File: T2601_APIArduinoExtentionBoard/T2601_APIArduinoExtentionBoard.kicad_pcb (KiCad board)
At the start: 4 copper layers, 59.8 x 90 mm, 100 parts, among them J1 Conn_01x10_Socket, J11 Conn_01x04_Pin, J12 Screw_Terminal_01x02, J13 Conn_01x04_Pin, J14 Screw_Terminal_01x02, J15 Conn_02x08_Counter_Clockwise, J2 Conn_01x10_Socket, J3 Conn_01x10_Socket, J4 Conn_01x10_Socket, J5 Screw_Terminal_01x08, J6 Screw_Terminal_01x08, J7 Conn_02x03_Counter_Clockwise, J8 Conn_01x04, J9 Conn_02x08_Counter_Clockwise, U2 ATmega328PB-A, X1 X322516MOB4SI

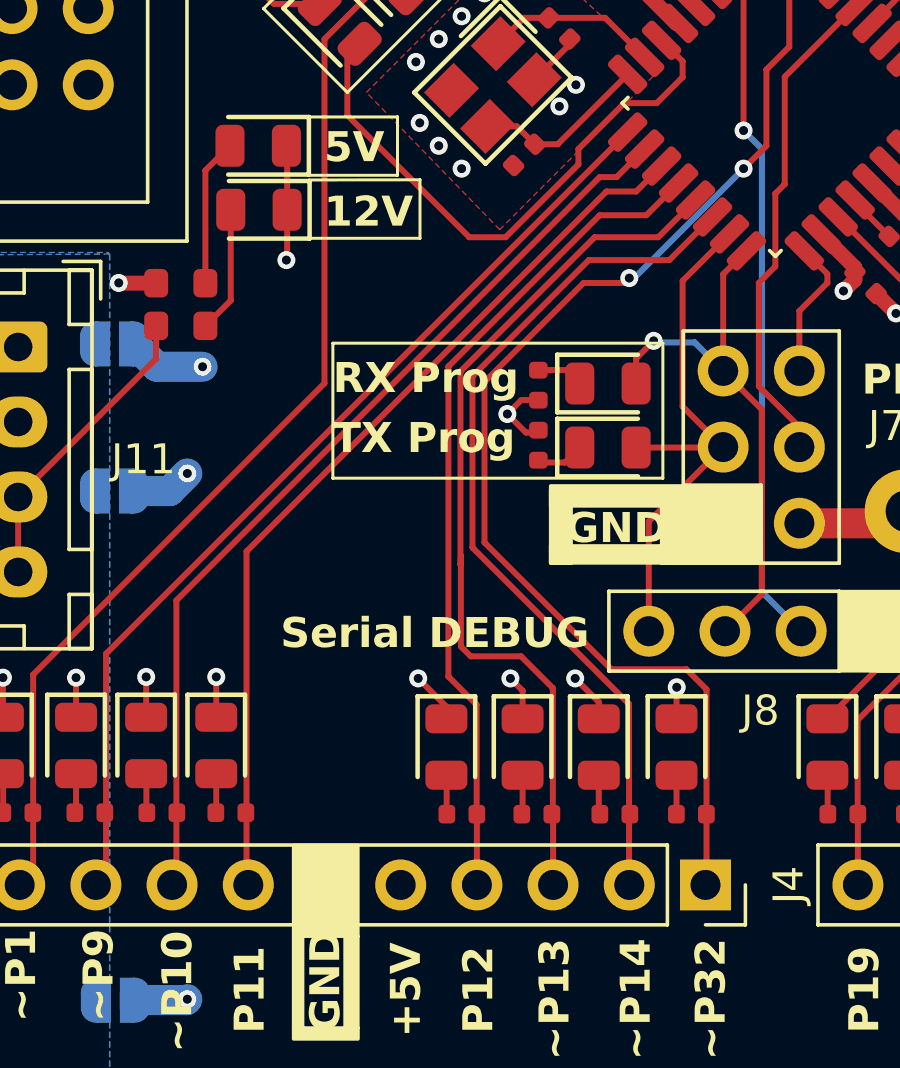
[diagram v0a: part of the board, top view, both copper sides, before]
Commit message: Modification affectation pin PWM Mezz 1
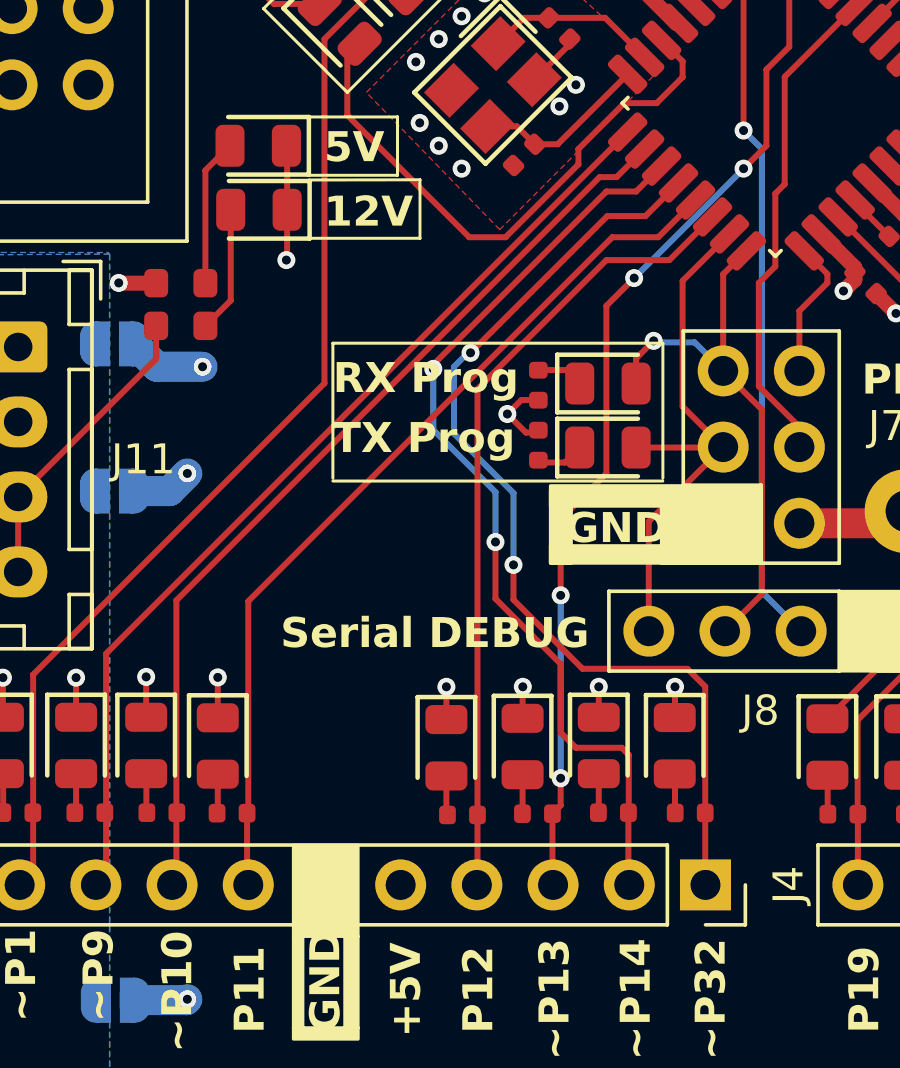
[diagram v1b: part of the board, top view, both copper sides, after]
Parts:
- moved D14 12.8 mm to (150.1, 78.4)
- moved R10 12.8 mm to (150.6, 80.7)
- moved D16 10.2 mm to (137.4, 78.4)
- moved R12 10.2 mm to (137.9, 80.7)
- moved D15 7.61 mm to (152.6, 78.4)
- moved R11 7.61 mm to (153.2, 80.7)
- moved D18 5.13 mm to (147.6, 78.4)
- moved R14 5.13 mm to (148.1, 80.7)
- moved D17 5.08 mm to (145.0, 78.5)
- moved R13 5.08 mm to (145.6, 80.7)
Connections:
- J4 pad 1: P32 -> P12
- J4 pad 2: P14 -> P11
- J4 pad 3: P13 -> P32
- J4 pad 4: P12 -> P14
- J4 pad 7: P11 -> P13
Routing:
- net P32: track 40.8 -> 34.5 mm, vias 2 -> 4
- net P12: track 27.9 -> 32.9 mm, vias 0 -> 2
- net P14: track 29.3 -> 26.7 mm
- net GND: track 79.5 -> 77.7 mm
- net P11: track 30.3 -> 31.3 mm, vias 0 -> 2

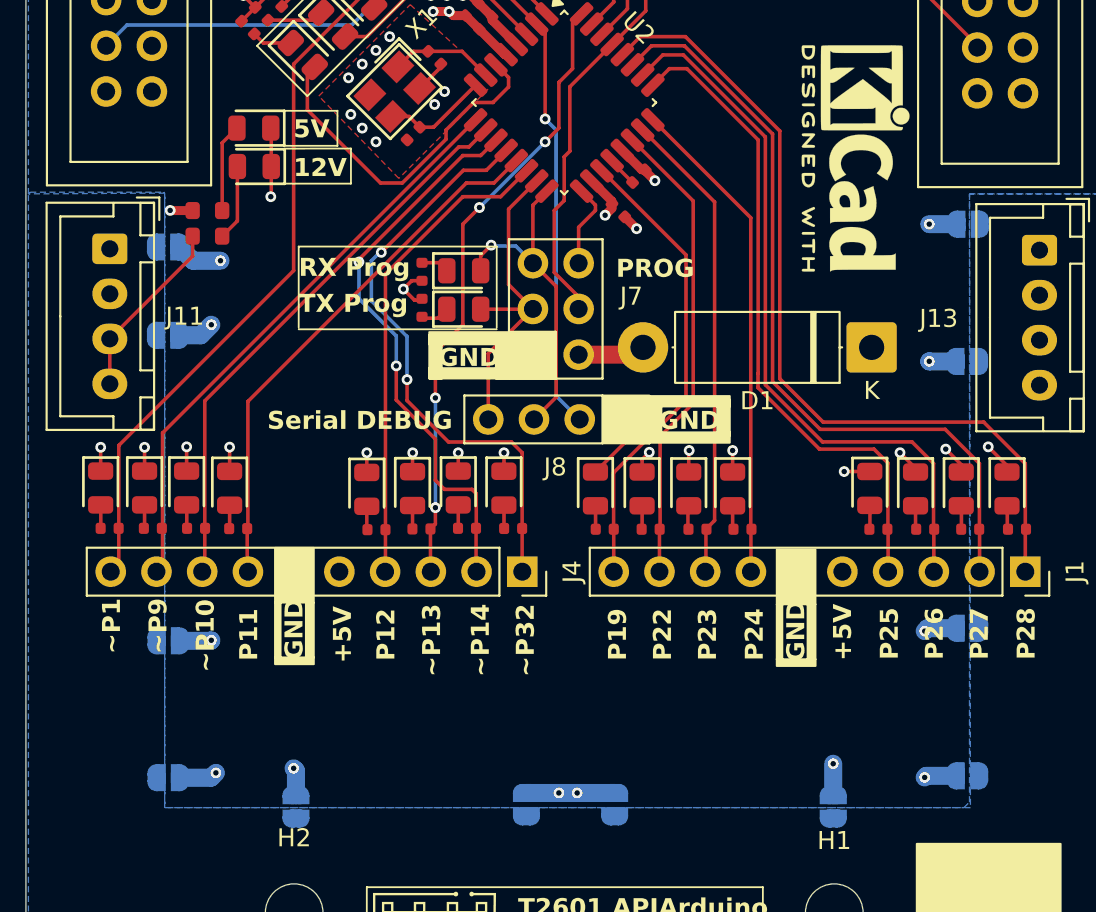
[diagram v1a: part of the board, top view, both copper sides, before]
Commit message: Modification issue #20 GND de la led 12V + ajout via entre In.1 et Bot pour la liaison des couches de GND
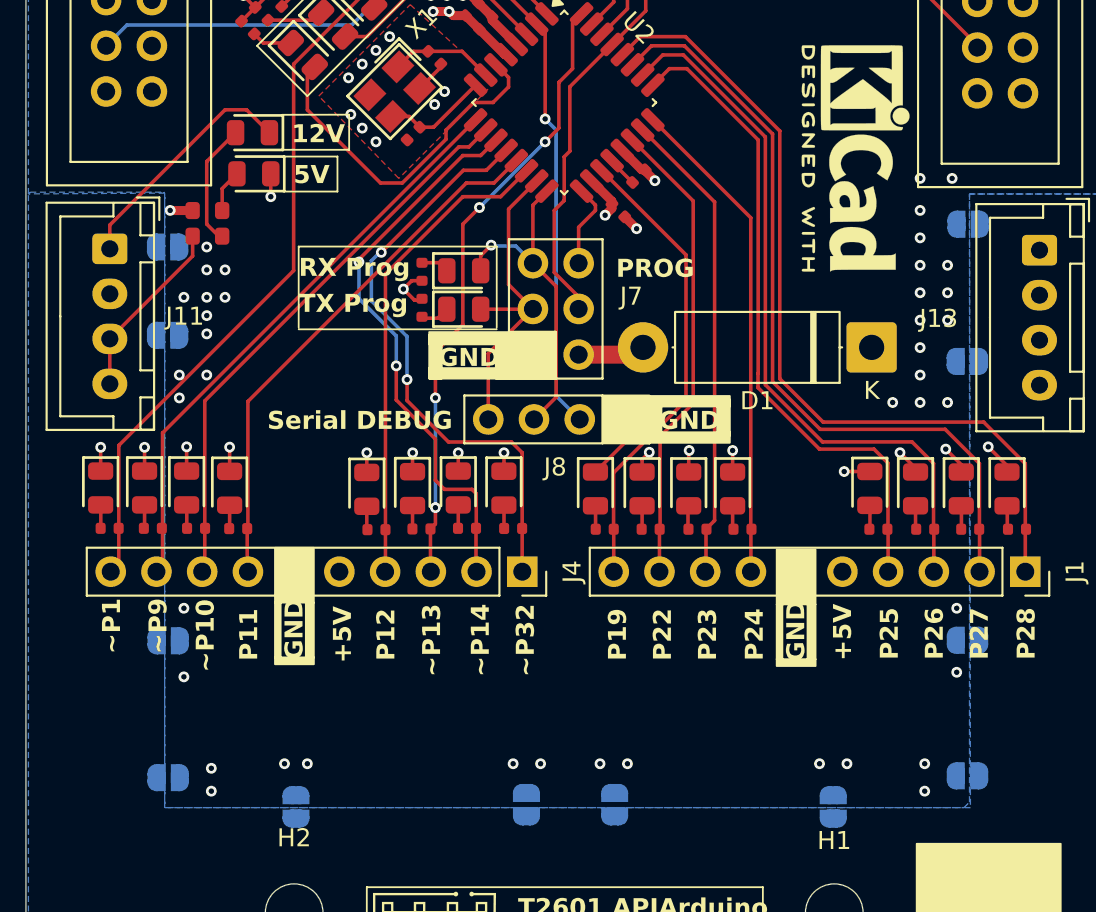
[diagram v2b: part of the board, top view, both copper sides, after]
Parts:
- moved D8 2.54 mm to (138.8, 61.0)
- moved D7 1.88 mm to (138.7, 58.7)
- moved JP7 0.67 mm to (178.4, 86.9)
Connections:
- D7 pad 1: GND -> GNDPWR
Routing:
- net GND: track 77.7 -> 51.9 mm, vias 45 -> 75
- net GNDPWR: track 0.00 -> 13.4 mm
- net Net-(D7-Pad2): track 4.22 -> 6.88 mm
- net Net-(D8-Pad2): track 4.92 -> 2.38 mm

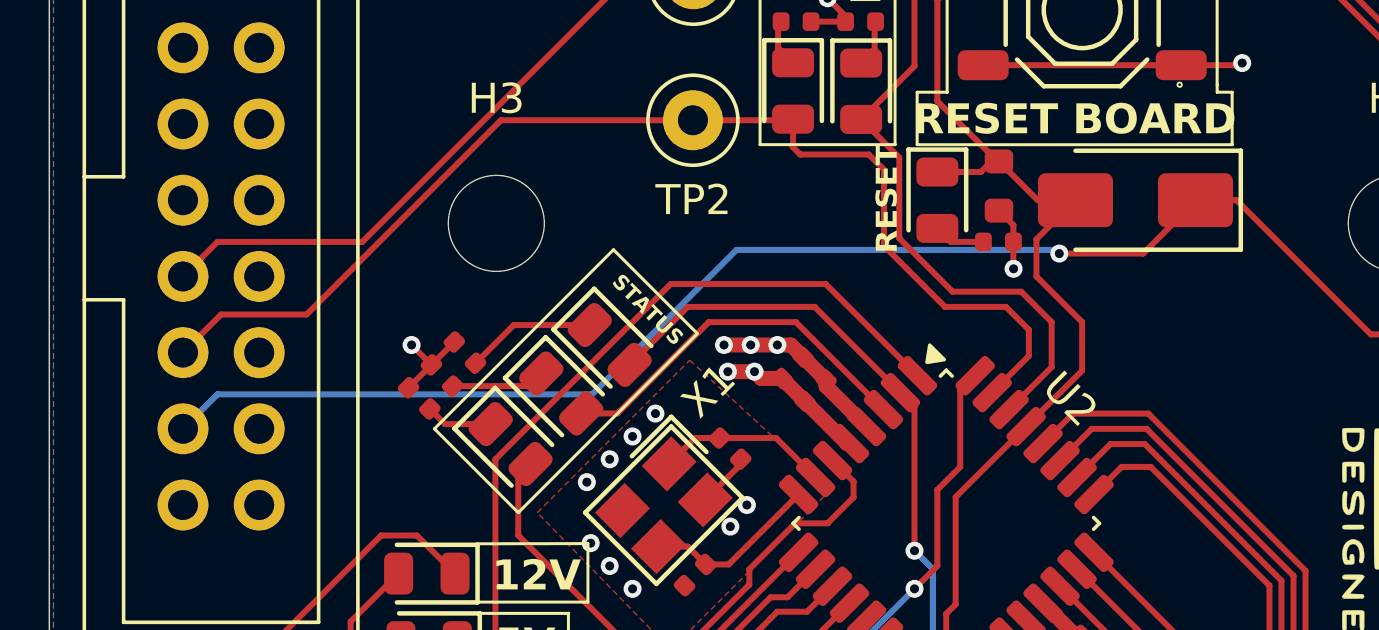
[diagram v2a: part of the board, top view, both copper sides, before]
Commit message: Piste de RESET general
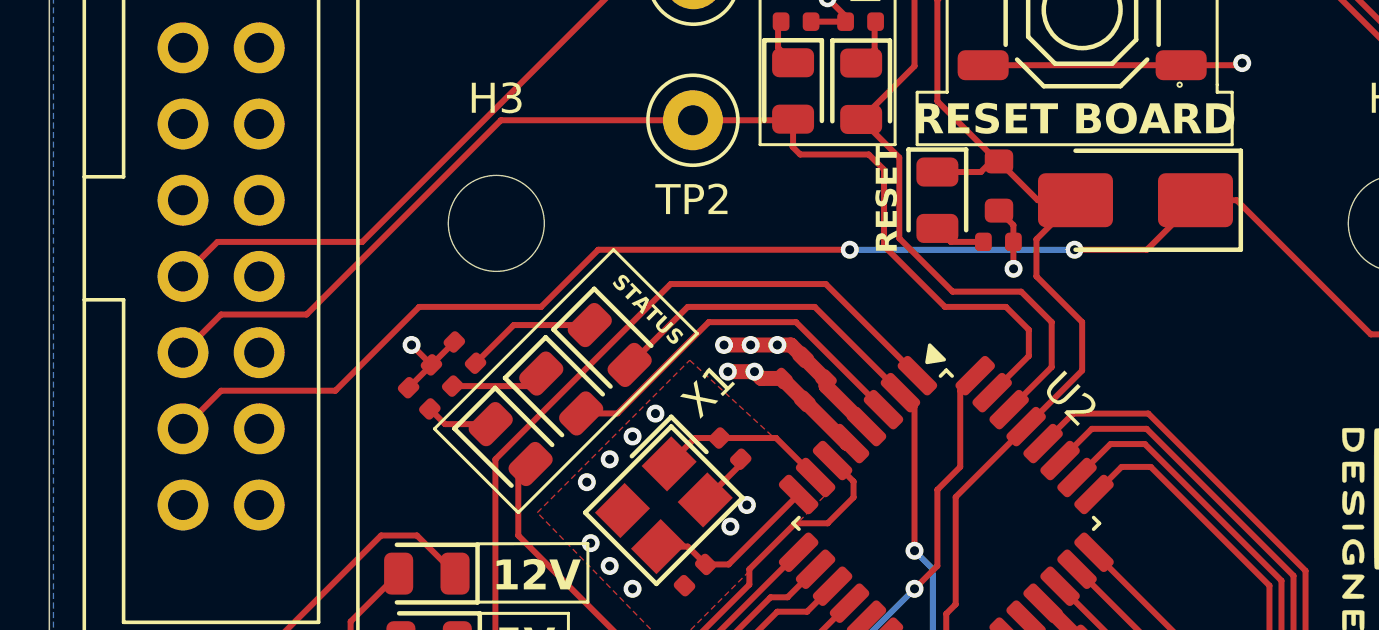
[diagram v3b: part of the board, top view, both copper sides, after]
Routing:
- net GEN_RESET: track 54.9 -> 54.8 mm, vias 1 -> 2
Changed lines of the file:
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@@
+	)
+	(segment
+		(start 160.274 47.879)
+		(end 162.687 47.879)
+		(width 0.2)
+		(layer "F.Cu")
+		(net "GEN_RESET")
+	)
+	(segment
+		(start 144.399 47.879)
+		(end 152.781 47.879)
+		(width 0.2)
+		(layer "F.Cu")
+		(net "GEN_RESET")
 	)
 	(segment
@@
 	)
 	(segment
-		(start 162.56 48.006)
-		(end 159.766 48.006)
+		(start 138.43 49.784)
+		(end 142.494 49.784)
+		(width 0.2)
+		(layer "F.Cu")
+		(net "GEN_RESET")
+	)
+	(segment
+		(start 142.494 49.784)
+		(end 144.399 47.879)
 		(width 0.2)
 		(layer "F.Cu")
@@
 	(segment
 		(start 164.306001 46.259999)
-		(end 162.56 48.006)
+		(end 162.687 47.879)
 		(width 0.2)
 		(layer "F.Cu")
@@
 		(start 170.15 50.7)
 		(end 165.678 46.228)
+		(width 0.2)
+		(layer "F.Cu")
+		(net "GEN_RESET")
+	)
+	(segment
+		(start 130.556 53.848)
+		(end 131.826 52.578)
+		(width 0.2)
+		(layer "F.Cu")
+		(net "GEN_RESET")
+	)
+	(segment
+		(start 131.826 52.578)
+		(end 135.636 52.578)
 		(width 0.2)
 		(layer "F.Cu")
@@
 	)
 	(segment
+		(start 135.636 52.578)
+		(end 138.43 49.784)
+		(width 0.2)
+		(layer "F.Cu")
+		(net "GEN_RESET")
+	)
+	(segment
 		(start 165.678 46.228)
 		(end 164.306001 46.228)
@@
 	)
 	(via
-		(at 159.766 48.006)
+		(at 152.781 47.879)
+		(size 0.6)
+		(drill 0.3)
+		(layers "F.Cu" "B.Cu")
+		(net "GEN_RESET")
+	)
+	(via
+		(at 160.274 47.879)
 		(size 0.6)
 		(drill 0.3)
@@
 	)
 	(segment
-		(start 131.706 52.698)
-		(end 130.556 53.848)
+		(start 152.781 47.879)
+		(end 160.274 47.879)
 		(width 0.2)
 		(layer "B.Cu")
-		(net "GEN_RESET")
-	)
-	(segment
-		(start 144.192471 52.698)
-		(end 131.706 52.698)
-		(width 0.2)
-		(layer "B.Cu")
-		(net "GEN_RESET")
-	)
-	(segment
-		(start 149.006096 47.884375)
-		(end 144.192471 52.698)
-		(width 0.2)
-		(layer "B.Cu")
-		(net "GEN_RESET")
-	)
-	(segment
-		(start 159.766 48.006)
-		(end 159.644375 47.884375)
-		(width 0.2)
-		(layer "B.Cu")
-		(net "GEN_RESET")
-	)
-	(segment
-		(start 159.644375 47.884375)
-		(end 149.006096 47.884375)
-		(width 0.2)
-		(layer "B.Cu")

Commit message: Modification connecteurs
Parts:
- renumbered J7 to J10, J8 to J11, J4 to J2, J15 to J20, J9 to J21, J11 to J30, J13 to J31, J2 to J4

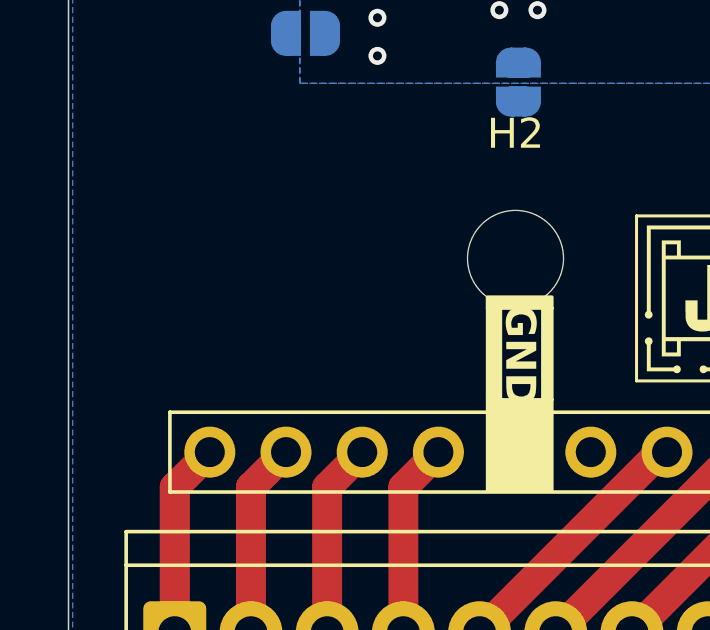
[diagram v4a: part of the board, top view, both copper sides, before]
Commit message: Ajouter Layer registration window
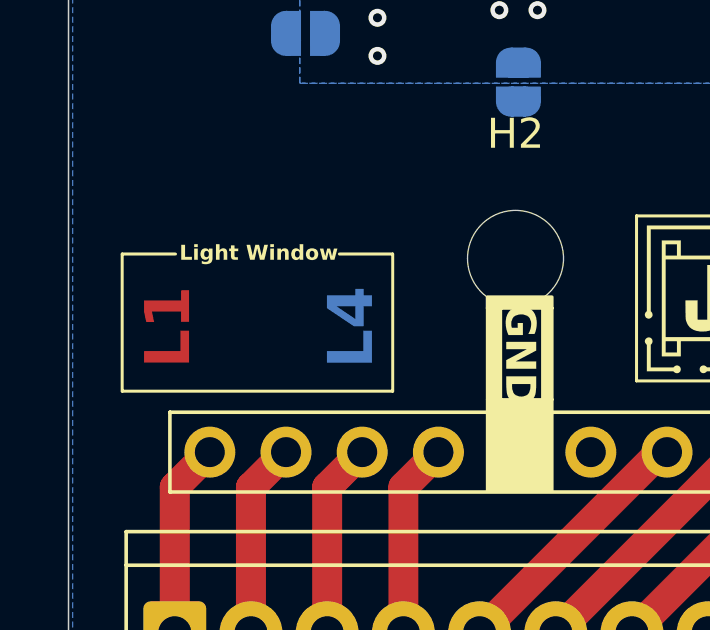
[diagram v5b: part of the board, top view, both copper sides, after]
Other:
- board text added: "L1"
- board text added: "L2"
- board text added: "L3"
- board text added: "L4"
- board text added: "Light Window"
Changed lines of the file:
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@@
 		)
 		(property "Value" "SolderJumper_2_Open"
-			(at 0 -1.9 0)
+			(at 6.230999 -7.212 90)
 			(layer "B.Fab")
 			(effects
@@
 	)
 	(gr_line
+		(start 127.889 101.854)
+		(end 127.889 106.426)
+		(stroke
+			(width 0.1)
+			(type default)
+		)
+		(layer "F.SilkS")
+	)
+	(gr_line
+		(start 127.889 106.426)
+		(end 136.906 106.426)
+		(stroke
+			(width 0.1)
+			(type default)
+		)
+		(layer "F.SilkS")
+	)
+	(gr_line
+		(start 129.667 101.854)
+		(end 127.889 101.854)
+		(stroke
+			(width 0.1)
+			(type default)
+		)
+		(layer "F.SilkS")
+	)
+	(gr_line
+		(start 135.128 101.854)
+		(end 136.906 101.854)
+		(stroke
+			(width 0.1)
+			(type default)
+		)
+		(layer "F.SilkS")
+	)
+	(gr_line
+		(start 136.906 101.854)
+		(end 136.906 106.426)
+		(stroke
+			(width 0.1)
+			(type default)
+		)
+		(layer "F.SilkS")
+	)
+	(gr_line
 		(start 138.938 53.848)
 		(end 144.907 47.879)
@@
 		(layer "Edge.Cuts")
 	)
+	(gr_text "L1\n"
+		(at 130.302 105.664 90)
+		(layer "F.Cu")
+		(effects
+			(font
+				(size 1.5 1.5)
+				(thickness 0.3)
+				(bold yes)
+			)
+			(justify left bottom)
+		)
+	)
 	(gr_text "\nCopyright (C) 2026 HackHype\nCERN OHL-S v2\n\n"
 		(at 154.91 37.72 0)
@@
 		)
 	)
+	(gr_text "L4\n"
+		(at 136.398 105.664 90)
+		(layer "B.Cu")
+		(effects
+			(font
+				(size 1.5 1.5)
+				(thickness 0.3)
+				(bold yes)
+			)
+			(justify left bottom)
+		)
+	)
+	(gr_text "L2\n"
+		(at 132.334 105.664 90)
+		(layer "In1.Cu")
+		(effects
+			(font
+				(size 1.5 1.5)
+				(thickness 0.3)
+				(bold yes)
+			)
+			(justify left bottom)
+		)
+	)
+	(gr_text "Light Window"
+		(at 129.794 102.108 0)
+		(layer "F.SilkS")
+		(effects
+			(font
+				(size 0.5 0.5)
+				(thickness 0.125)
+				(bold yes)
+			)
+			(justify left bottom)
+		)
+	)
 	(gr_text "STATUS\n"
 		(at 144.78 49.022 315)
@@
 		)
 	)
+	(gr_text "L3\n"
+		(at 134.366 105.664 90)
+		(layer "In2.Cu")
+		(effects
+			(font
+				(size 1.5 1.5)
+				(thickness 0.3)
+				(bold yes)
+			)
+			(justify left bottom)
+		)
+	)
 	(segment
 		(start 139.545553 52.423553)
@@
 			)
 		)
+	)
+	(zone
+		(layers "F.Cu" "B.Cu" "In1.Cu" "In2.Cu")
+		(hatch edge 0.5)
+		(connect_pads
+			(clearance 0)
+		)
+		(min_thickness 0.25)
+		(keepout
+			(tracks not_allowed)
+			(vias not_allowed)
+			(pads not_allowed)
+			(copperpour not_allowed)
+			(footprints allowed)
+		)
+		(placement
+			(enabled no)
+			(sheetname "")
+		)
+		(fill
+			(thermal_gap 0.5)
+			(thermal_bridge_width 0.5)
+			(island_removal_mode 0)
+		)
+		(polygon
+			(pts
+				(xy 128.143 106.172) (xy 128.143 102.362) (xy 136.652001 102.362) (xy 136.652 106.172)
+			)
+		)
+	)
+	(zone
+		(layers "*.Mask")
+		(hatch edge 0.5)
+		(connect_pads
+			(clearance 0)
+		)
+		(min_thickness 0.25)
+		(fill yes
+			(thermal_gap 0.5)
+			(thermal_bridge_width 0.5)
+			(island_removal_mode 0)
+		)
+		(polygon
+			(pts
+				(xy 136.779 106.172) (xy 136.779 102.362) (xy 128.143 102.362) (xy 128.143 106.172)
+			)
+		)
